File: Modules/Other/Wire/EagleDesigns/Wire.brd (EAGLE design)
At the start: 100 x 80 mm, 2 parts

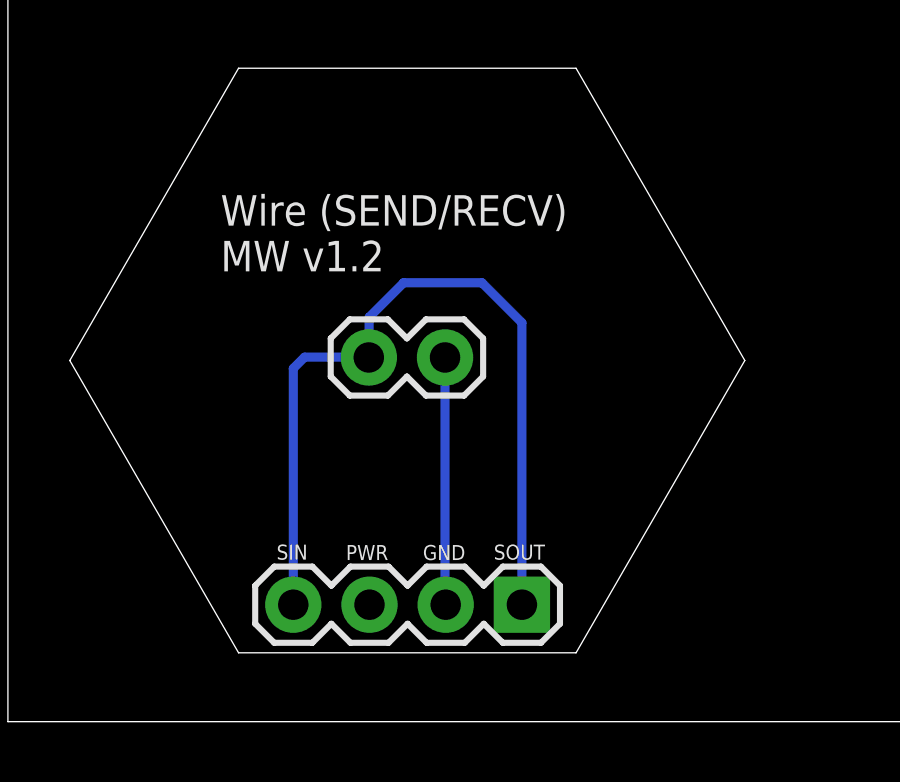
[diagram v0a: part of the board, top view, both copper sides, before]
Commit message: Added one single Board Layout for WireSEND, WireRECV, and Dummy module
it now has a small jumper that could be soldered in order to connect
SIN to SOUT.
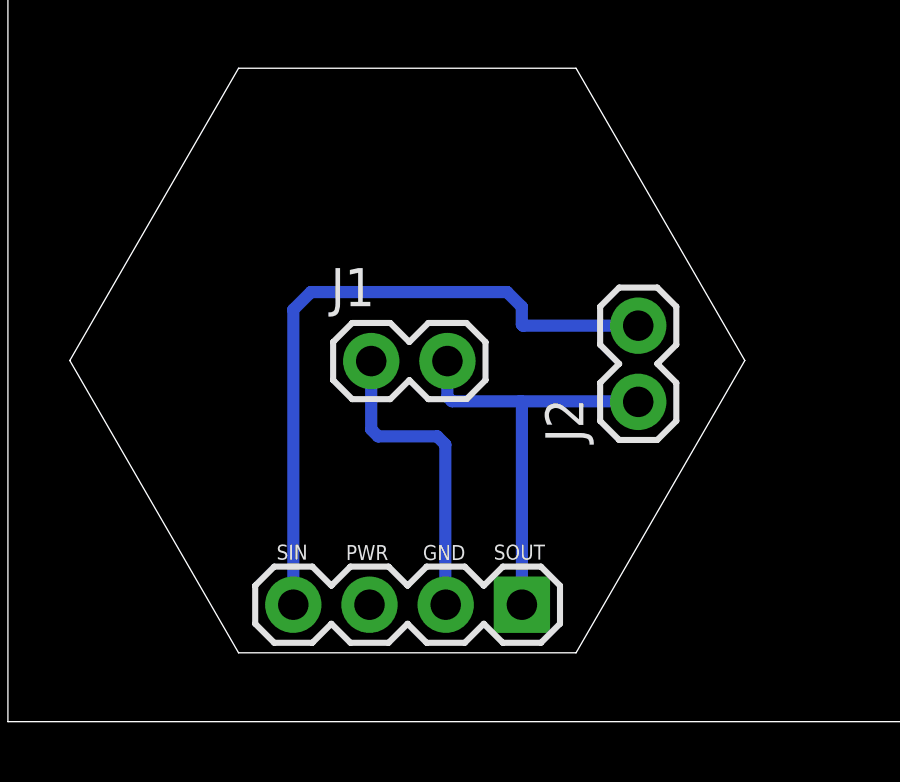
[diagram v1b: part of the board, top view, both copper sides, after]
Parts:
- added J2: (no value), SparkFun-Connectors:1X02
- moved J1 2.46 mm to (12.1, 12.0), turned to 0 degrees
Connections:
- removed net 1X3SIN-SOUT: J1.2, JP1.1, JP1.4
- new net SIN: J2.2, JP1.4
- new net SOUT: J1.2, J2.1, JP1.1
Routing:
- net 1X3SIN-SOUT: track 27.4 -> 0.00 mm
- net SIN: track 0.00 -> 22.4 mm
- net SOUT: track 0.00 -> 14.4 mm
- net GND: track 8.25 -> 10.4 mm
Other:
- board text removed: "Wire (SEND/RECV) MW v1.2"
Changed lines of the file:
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@@
 <layer number="24" name="bOrigins" color="15" fill="1" visible="yes" active="yes"/>
 <layer number="25" name="tNames" color="7" fill="1" visible="yes" active="yes"/>
-<layer number="26" name="bNames" color="7" fill="1" visible="yes" active="yes"/>
+<layer number="26" name="bNames" color="7" fill="1" visible="no" active="yes"/>
 <layer number="27" name="tValues" color="7" fill="1" visible="yes" active="yes"/>
 <layer number="28" name="bValues" color="7" fill="1" visible="yes" active="yes"/>
@@
 <text x="13.8323" y="5.388" size="0.5" layer="21">GND</text>
 <text x="16.1945" y="5.4007" size="0.5" layer="21">SOUT</text>
-<text x="7.09" y="15.01" size="1.016" layer="21">Wire (SEND/RECV)
-MW v1.2</text>
 </plain>
 <attributes>
@@
 <attribute name="VALUE" x="18.4023" y="7.0739" size="1.27" layer="27" rot="R180"/>
 </element>
-<element name="J1" library="SparkFun-Connectors" package="1X02" value="" x="14.57" y="12.14" smashed="yes" rot="R180">
-<attribute name="VALUE" x="15.84" y="15.315" size="1.27" layer="27" rot="R180"/>
-</element>
+<element name="J2" library="SparkFun-Connectors" package="1X02" value="" x="21.01" y="10.66" rot="R90"/>
+<element name="J1" library="SparkFun-Connectors" package="1X02" value="" x="12.11" y="12.02"/>
 </elements>
 <signals>
@@
 <signal name="GND">
 <contactref element="JP1" pad="2"/>
+<wire x1="14.55" y1="3.9412" x2="14.5923" y2="3.8989" width="0.3048" layer="16"/>
 <contactref element="J1" pad="1"/>
-<wire x1="14.57" y1="12.14" x2="14.57" y2="3.9212" width="0.3048" layer="16"/>
-<wire x1="14.57" y1="3.9212" x2="14.5923" y2="3.8989" width="0.3048" layer="16"/>
+<wire x1="12.11" y1="12.02" x2="12.11" y2="9.74" width="0.4064" layer="16"/>
+<wire x1="12.11" y1="9.74" x2="12.34" y2="9.51" width="0.4064" layer="16"/>
+<wire x1="12.34" y1="9.51" x2="14.31" y2="9.51" width="0.4064" layer="16"/>
+<wire x1="14.31" y1="9.51" x2="14.58" y2="9.24" width="0.4064" layer="16"/>
+<wire x1="14.58" y1="9.24" x2="14.58" y2="3.9112" width="0.4064" layer="16"/>
+<wire x1="14.58" y1="3.9112" x2="14.5923" y2="3.8989" width="0.4064" layer="16"/>
 </signal>
-<signal name="1X3SIN-SOUT">
+<signal name="SIN">
 <contactref element="JP1" pad="4"/>
+<contactref element="J2" pad="2"/>
+<wire x1="9.5123" y1="3.8989" x2="9.5123" y2="13.7323" width="0.4064" layer="16"/>
+<wire x1="9.5123" y1="13.7323" x2="10.1" y2="14.32" width="0.4064" layer="16"/>
+<wire x1="10.1" y1="14.32" x2="16.64" y2="14.32" width="0.4064" layer="16"/>
+<wire x1="16.64" y1="14.32" x2="17.13" y2="13.83" width="0.4064" layer="16"/>
+<wire x1="17.13" y1="13.83" x2="17.13" y2="13.24" width="0.4064" layer="16"/>
+<wire x1="17.13" y1="13.24" x2="17.17" y2="13.2" width="0.4064" layer="16"/>
+<wire x1="17.17" y1="13.2" x2="21.01" y2="13.2" width="0.4064" layer="16"/>
+</signal>
+<signal name="SOUT">
 <contactref element="JP1" pad="1"/>
+<contactref element="J2" pad="1"/>
 <contactref element="J1" pad="2"/>
-<wire x1="9.5123" y1="3.8989" x2="9.5123" y2="11.7723" width="0.3048" layer="16"/>
-<wire x1="9.5123" y1="11.7723" x2="9.89" y2="12.15" width="0.3048" layer="16"/>
-<wire x1="9.89" y1="12.15" x2="12.02" y2="12.15" width="0.3048" layer="16"/>
-<wire x1="12.02" y1="12.15" x2="12.03" y2="12.14" width="0.3048" layer="16"/>
-<wire x1="17.1323" y1="3.8989" x2="17.1323" y2="13.2977" width="0.3048" layer="16"/>
-<wire x1="17.1323" y1="13.2977" x2="15.8" y2="14.63" width="0.3048" layer="16"/>
-<wire x1="15.8" y1="14.63" x2="13.19" y2="14.63" width="0.3048" layer="16"/>
-<wire x1="13.19" y1="14.63" x2="12.04" y2="13.48" width="0.3048" layer="16"/>
-<wire x1="12.04" y1="13.48" x2="12.04" y2="12.15" width="0.3048" layer="16"/>
-<wire x1="12.04" y1="12.15" x2="12.03" y2="12.14" width="0.3048" layer="16"/>
+<wire x1="14.65" y1="12.02" x2="14.65" y2="10.83" width="0.4064" layer="16"/>
+<wire x1="14.65" y1="10.83" x2="14.8" y2="10.68" width="0.4064" layer="16"/>
+<wire x1="14.8" y1="10.68" x2="17.09" y2="10.68" width="0.4064" layer="16"/>
+<wire x1="17.09" y1="10.68" x2="20.99" y2="10.68" width="0.4064" layer="16"/>
+<wire x1="20.99" y1="10.68" x2="21.01" y2="10.66" width="0.4064" layer="16"/>
+<wire x1="17.1323" y1="3.8989" x2="17.1323" y2="10.6377" width="0.4064" layer="16"/>
+<wire x1="17.1323" y1="10.6377" x2="17.09" y2="10.68" width="0.4064" layer="16"/>
 </signal>
 </signals>
@@
 </board>
 </drawing>
-<compatibility>
-<note version="6.3" minversion="6.2.2" severity="warning">
-Since Version 6.2.2 text objects can contain more than one line,
-which will not be processed correctly with this version.
-</note>
-</compatibility>
 </eagle>
